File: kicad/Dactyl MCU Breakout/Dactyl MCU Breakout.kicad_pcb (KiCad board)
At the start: 2 copper layers, 54.5 x 62.1 mm, 37 parts, among them J202 Split, J203 Column, J204 Thumb, J205 External, J206 Row, J207 Display, J208 Vic, J209 JST, SW201 Battery, SW202 Reset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

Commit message: feat: four layer PCB, inners GND. Reconnect GNDs.
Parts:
- moved JP201 0.67 mm to (109.5, 84.6)
- moved JP204 0.50 mm to (122.2, 92.4)
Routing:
- net GND: track 45.6 -> 23.0 mm, vias 36 -> 32
- net /Right/RAW_ENABLED: track 3.04 -> 3.58 mm
- added copper zone on In1.Cu, net GND
- added copper zone on In2.Cu, net GND
- removed copper zone on B.Cu, net GND
- removed copper zone on F.Cu, net GND
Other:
- copper layers 2 -> 4
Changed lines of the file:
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@@
 	(layers
 		(0 "F.Cu" signal)
+		(1 "In1.Cu" power)
+		(2 "In2.Cu" power)
 		(31 "B.Cu" signal)
 		(32 "B.Adhes" user "B.Adhesive")
@@
 			)
 			(layer "dielectric 1"
+				(type "prepreg")
+				(thickness 0.1)
+				(material "FR4")
+				(epsilon_r 4.5)
+				(loss_tangent 0.02)
+			)
+			(layer "In1.Cu"
+				(type "copper")
+				(thickness 0.035)
+			)
+			(layer "dielectric 2"
 				(type "core")
-				(thickness 1.51)
+				(thickness 1.24)
+				(material "FR4")
+				(epsilon_r 4.5)
+				(loss_tangent 0.02)
+			)
+			(layer "In2.Cu"
+				(type "copper")
+				(thickness 0.035)
+			)
+			(layer "dielectric 3"
+				(type "prepreg")
+				(thickness 0.1)
 				(material "FR4")
 				(epsilon_r 4.5)
@@
 		(fp_arc
 			(start 6.938123 15.132041)
-			(mid 6.337062 14.8831)
+			(mid 6.337066 14.8831)
 			(end 6.088123 14.282041)
 			(stroke
@@
 		(fp_arc
 			(start 8.236041 -15.740877)
-			(mid 8.837086 -15.491923)
+			(mid 8.837089 -15.491924)
 			(end 9.086041 -14.890877)
 			(stroke
@@
 	(footprint "Dactyl_basics:SolderJumper-2_P1.3mm_Open_RoundedPad1.0x1.5mm"
 		(layer "B.Cu")
-		(at 122.2 92.9 180)
+		(at 122.15 92.4 180)
 		(descr "SMD Solder Jumper, 1x1.5mm, rounded Pads, 0.3mm gap, open")
 		(tags "solder jumper open")
@@
 	(footprint "Dactyl_basics:SolderJumper-2_P1.3mm_Open_RoundedPad1.0x1.5mm"
 		(layer "B.Cu")
-		(at 108.9 84.3 90)
+		(at 109.5 84.6 90)
 		(descr "SMD Solder Jumper, 1x1.5mm, rounded Pads, 0.3mm gap, open")
 		(tags "solder jumper open")
@@
 	)
 	(segment
-		(start 123.5364 56.362)
-		(end 120.938 56.362)
+		(start 121.45 93.95)
+		(end 121.455 93.955)
+		(width 0.381)
+		(layer "F.Cu")
+		(net 2)
+	)
+	(segment
+		(start 105.45 95)
+		(end 104.1625 95)
+		(width 0.381)
+		(layer "F.Cu")
+		(net 2)
+	)
+	(segment
+		(start 105.545 91.85)
+		(end 108.15 91.85)
 		(width 0.381)
 		(layer "F.Cu")
@@
 	)
 	(segment
-		(start 120.9 56.2)
+		(start 120.9 56.5)
 		(end 120.9 55.58)
 		(width 0.381)
@@
 	)
 	(segment
-		(start 118.8 56.35)
-		(end 118.8 57)
+		(start 126.4 101.325305)
+		(end 126.4 102.65)
 		(width 0.381)
 		(layer "F.Cu")
@@
 	)
 	(segment
+		(start 107.4 85.35)
+		(end 105.545 85.35)
+		(width 0.381)
+		(layer "F.Cu")
+		(net 2)
+	)
+	(segment
 		(start 112.2375 80.1)
 		(end 113.8 80.1)
@@
 	)
 	(segment
-		(start 112.65 74.04)
-		(end 112.59 74.1)
+		(start 126.369696 101.295001)
+		(end 126.4 101.325305)
 		(width 0.381)
 		(layer "F.Cu")
@@
 	)
 	(segment
-		(start 120.938 56.362)
-		(end 120.9 56.4)
+		(start 101.5 80.7)
+		(end 100.7 80.7)
 		(width 0.381)
 		(layer "F.Cu")
@@
 	)
 	(segment
-		(start 119.1 57.3)
-		(end 119.8 57.3)
+		(start 127.7 62.8)
+		(end 126.78 62.8)
 		(width 0.381)
 		(layer "F.Cu")
@@
 	)
 	(segment
-		(start 118.8 57)
-		(end 119.1 57.3)
+		(start 108.1 84.65)
+		(end 107.4 85.35)
 		(width 0.381)
 		(layer "F.Cu")
@@
 	)
 	(segment
-		(start 112.59 74.1)
-		(end 107.325 74.1)
+		(start 118.8 57.5)
+		(end 118.8 56.35)
+		(width 0.381)
+		(layer "F.Cu")
+		(net 2)
+	)
+	(segment
+		(start 128.5 95.325)
+		(end 128.5 94.05)
 		(width 0.381)
 		(layer "F.Cu")
@@
 	)
 	(segment
-		(start 119.8 57.3)
-		(end 120.9 56.2)
+		(start 121.455 93.955)
+		(end 121.455 95.325)
 		(width 0.381)
 		(layer "F.Cu")
@@
 	)
 	(via
-		(at 138.9 103.65)
-		(size 0.8)
-		(drill 0.4)
-		(layers "F.Cu" "B.Cu")
-		(free yes)
-		(net 2)
-	)
-	(via
 		(at 114.7 81.6)
 		(size 0.8)
@@
 	)
 	(via
-		(at 132.2 60.25)
-		(size 0.8)
-		(drill 0.4)
-		(layers "F.Cu" "B.Cu")
-		(free yes)
-		(net 2)
-	)
-	(via
-		(at 119.75 96)
+		(at 121.45 93.95)
 		(size 0.8)
 		(drill 0.4)
@@
 	)
 	(via
-		(at 125.3 99.3)
+		(at 126.369696 101.295001)
 		(size 0.8)
 		(drill 0.4)
@@
 	)
 	(via
-		(at 132.2 58)
+		(at 105.45 95)
 		(size 0.8)
 		(drill 0.4)
@@
 	)
 	(via
-		(at 112.65 74.04)
+		(at 107.325 74.1)
 		(size 0.8)
 		(drill 0.4)
@@
 	)
 	(via
-		(at 101.85 79)
+		(at 100.7 80.7)
 		(size 0.8)
 		(drill 0.4)
@@
 	)
 	(via
-		(at 126.675 95.15)
+		(at 128.5 94.05)
 		(size 0.8)
 		(drill 0.4)
@@
 	)
 	(via
-		(at 122.8 90.4)
+		(at 120.9 56.5)
 		(size 0.8)
 		(drill 0.4)
@@
 	)
 	(via
-		(at 147.9 93.1)
+		(at 122.8 90.4)
 		(size 0.8)
 		(drill 0.4)
@@
 	)
 	(via
-		(at 128.6 60.25)
+		(at 147.9 93.1)
 		(size 0.8)
 		(drill 0.4)
@@
 	)
 	(via
-		(at 108.75 93.9)
+		(at 108.15 91.85)
 		(size 0.8)
 		(drill 0.4)
@@
 	)
 	(via
-		(at 101.75 88.65)
+		(at 108.1 84.65)
 		(size 0.8)
 		(drill 0.4)
@@
 	)
 	(via
-		(at 132.2 54.6)
-		(size 0.8)
-		(drill 0.4)
-		(layers "F.Cu" "B.Cu")
-		(free yes)
-		(net 2)
-	)
-	(via
-		(at 138.9 99.15)
+		(at 118.8 57.5)
 		(size 0.8)
 		(drill 0.4)
@@
 	)
 	(via
-		(at 116.4 57.1)
-		(size 0.8)
-		(drill 0.4)
-		(layers "F.Cu" "B.Cu")
-		(free yes)
-		(net 2)
-	)
-	(via
-		(at 126.7 60.25)
+		(at 127.7 62.8)
 		(size 0.8)
 		(drill 0.4)
@@
 	)
 	(segment
-		(start 123.5364 56.362)
-		(end 121.363 56.362)
-		(width 0.381)
-		(layer "B.Cu")
-		(net 2)
-	)
-	(segment
-		(start 121.363 56.362)
-		(end 120 57.725)
-		(width 0.381)
-		(layer "B.Cu")
-		(net 2)
-	)
-	(segment
-		(start 113.72 64.88)
-		(end 116.4 64.88)
-		(width 0.381)
-		(layer "B.Cu")
-		(net 2)
-	)
-	(segment
-		(start 112.675 74.015)
-		(end 112.675 65.925)
-		(width 0.381)
-		(layer "B.Cu")
-		(net 2)
-	)
-	(segment
-		(start 112.675 65.925)
-		(end 113.72 64.88)
-		(width 0.381)
-		(layer "B.Cu")
-		(net 2)
-	)
-	(segment
-		(start 116.6 64.88)
-		(end 116.4 64.88)
-		(width 0.381)
-		(layer "B.Cu")
-		(net 2)
-	)
-	(segment
-		(start 120 57.725)
-		(end 120 61.48)
-		(width 0.381)
-		(layer "B.Cu")
-		(net 2)
-	)
-	(segment
-		(start 112.65 74.04)
-		(end 112.675 74.015)
-		(width 0.381)
-		(layer "B.Cu")
-		(net 2)
-	)
-	(segment
-		(start 120 61.48)
-		(end 116.6 64.88)
-		(width 0.381)
-		(layer "B.Cu")
-		(net 2)
-	)
-	(segment
 		(start 115.185 101.65)
 		(end 113.38 103.455)
@@
 	)
 	(segment
-		(start 120.7 92.9)
-		(end 121.55 92.9)
-		(width 0.25)
-		(layer "B.Cu")
-		(net 5)
-	)
-	(segment
 		(start 102 72)
 		(end 101.675 71.675)
@@
 	)
 	(segment
+		(start 118.2 95.1)
+		(end 120.9 92.4)
+		(width 0.25)
+		(layer "B.Cu")
+		(net 5)
+	)
+	(segment
 		(start 118.2 97.5)
-		(end 115 100.7)
+		(end 118.2 95.1)
 		(width 0.25)
 		(layer "B.Cu")
@@
 	(segment
 		(start 118.2 97.5)
-		(end 118.2 95.4)
+		(end 115 100.7)
 		(width 0.25)
 		(layer "B.Cu")
@@
 	)
 	(segment
-		(start 118.2 95.4)
-		(end 120.7 92.9)
+		(start 120.9 92.4)
+		(end 121.5 92.4)
 		(width 0.25)
 		(layer "B.Cu")
@@
 	)
 	(segment
-		(start 108.35 86.15)
-		(end 108.9 85.6)
+		(start 108.3 86.15)
+		(end 109.25 86.15)
 		(width 0.381)
 		(layer "B.Cu")
@@
 	)
 	(segment
-		(start 108.9 85.6)
-		(end 108.9 84.95)
+		(start 109.5 85.9)
+		(end 109.5 85.25)
 		(width 0.381)
 		(layer "B.Cu")
@@
 	)
 	(segment
-		(start 108.3 86.15)
-		(end 108.35 86.15)
+		(start 109.25 86.15)
+		(end 109.5 85.9)
 		(width 0.381)
 		(layer "B.Cu")
@@
 	(segment
 		(start 126.1 92.9)
-		(end 122.85 92.9)
+		(end 125.6 92.4)
+		(width 0.25)
+		(layer "B.Cu")
+		(net 37)
+	)
+	(segment
+		(start 125.6 92.4)
+		(end 122.8 92.4)
 		(width 0.25)
 		(layer "B.Cu")
@@
 	)
 	(segment
-		(start 108.9 82.2)
+		(start 109.5 82.8)
 		(end 108.8 82.1)
 		(width 0.381)
@@
 	)
 	(segment
-		(start 108.9 83.65)
-		(end 108.9 82.2)
+		(start 109.5 83.95)
+		(end 109.5 82.8)
 		(width 0.381)
 		(layer "B.Cu")
@@
 		(net_name "GND")
 		(locked yes)
-		(layers "F&B.Cu")
+		(layers "In1.Cu" "In2.Cu")
 		(name "GND")
 		(hatch edge 0.5)

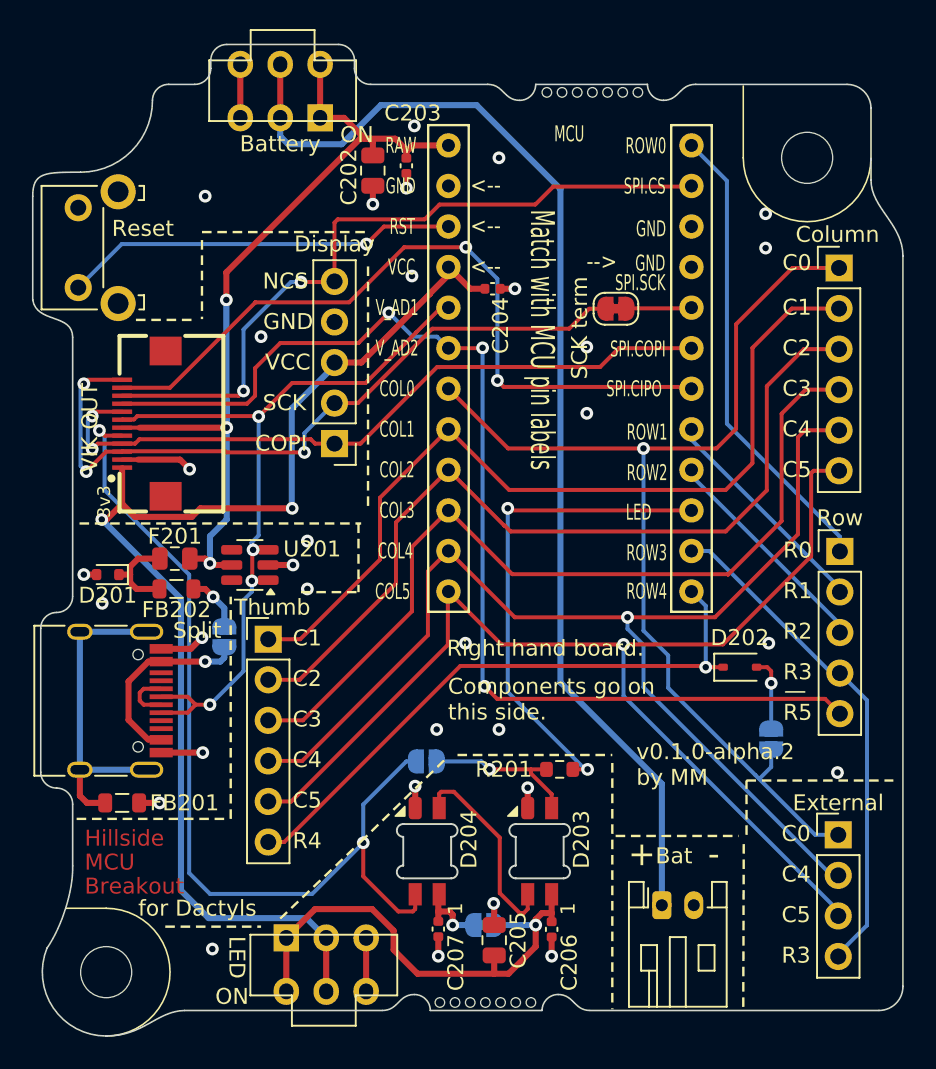
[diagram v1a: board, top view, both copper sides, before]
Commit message: feat: simplify traces, reduce trace vias. stitch
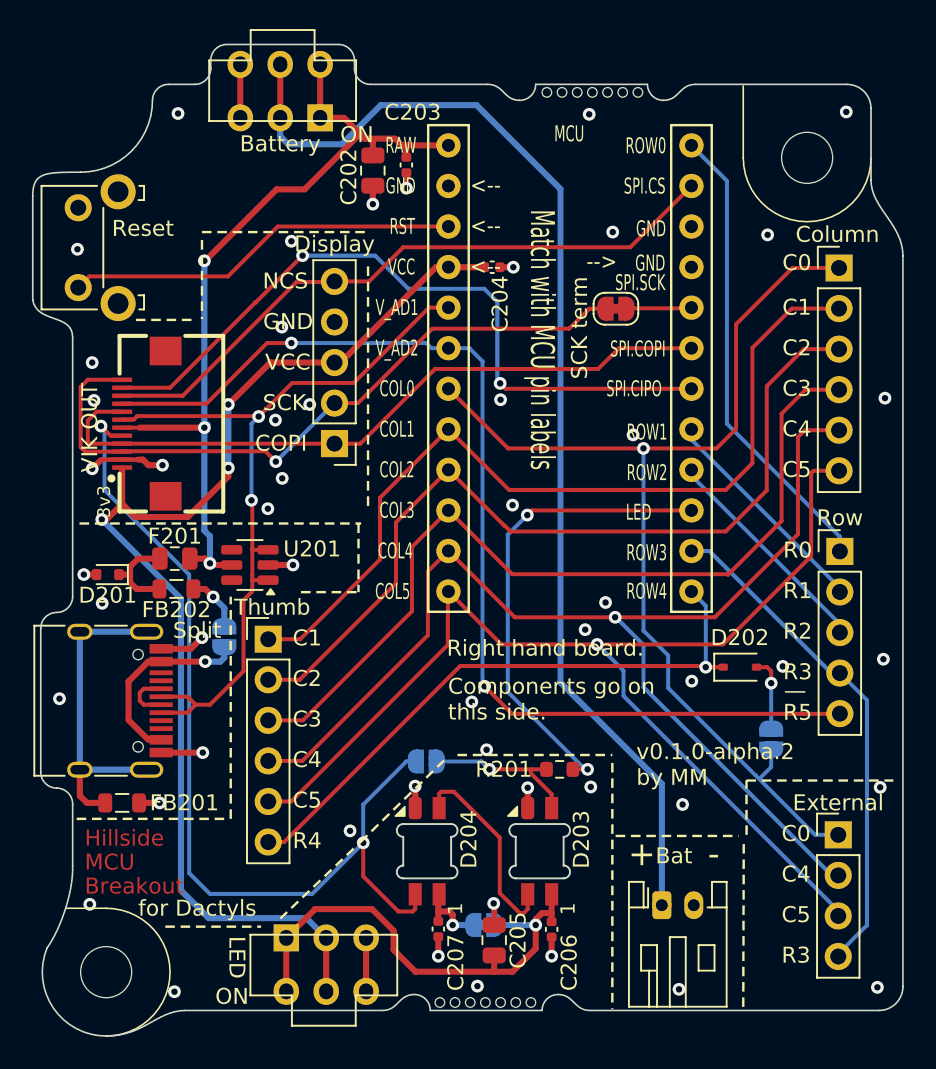
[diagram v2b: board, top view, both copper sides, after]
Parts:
- moved C204 1.35 mm to (126.3, 61.5)
- moved C203 0.05 mm to (120.9, 55.0)
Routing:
- net /Right/SPI0.SC: track 45.5 -> 41.1 mm, vias 2 -> 0
- net /Right/row5_VIK_GP_AD2: track 71.1 -> 68.0 mm, vias 3 -> 2
- net /Right/VCC: track 73.5 -> 71.3 mm, vias 2 -> 3
- net /Right/SPI0.SCK/SDA: track 45.8 -> 43.8 mm, vias 3 -> 1
- net /Right/RAW: track 52.8 -> 51.0 mm
- net /Right/SPI0.CIPO: track 46.7 -> 45.4 mm
- net /Right/LED: track 31.1 -> 29.9 mm
- net /Right/col5: track 74.6 -> 75.3 mm
- net /Right/SPI0.COPI/SCL: track 44.7 -> 44.1 mm, vias 2 -> 0
- net GND: track 23.0 -> 23.3 mm, vias 32 -> 51
- net /Right/SPLIT_VIK_GP_AD1: track 50.2 -> 50.3 mm, vias 4 -> 2
- net /Right/RST: vias 1 -> 0

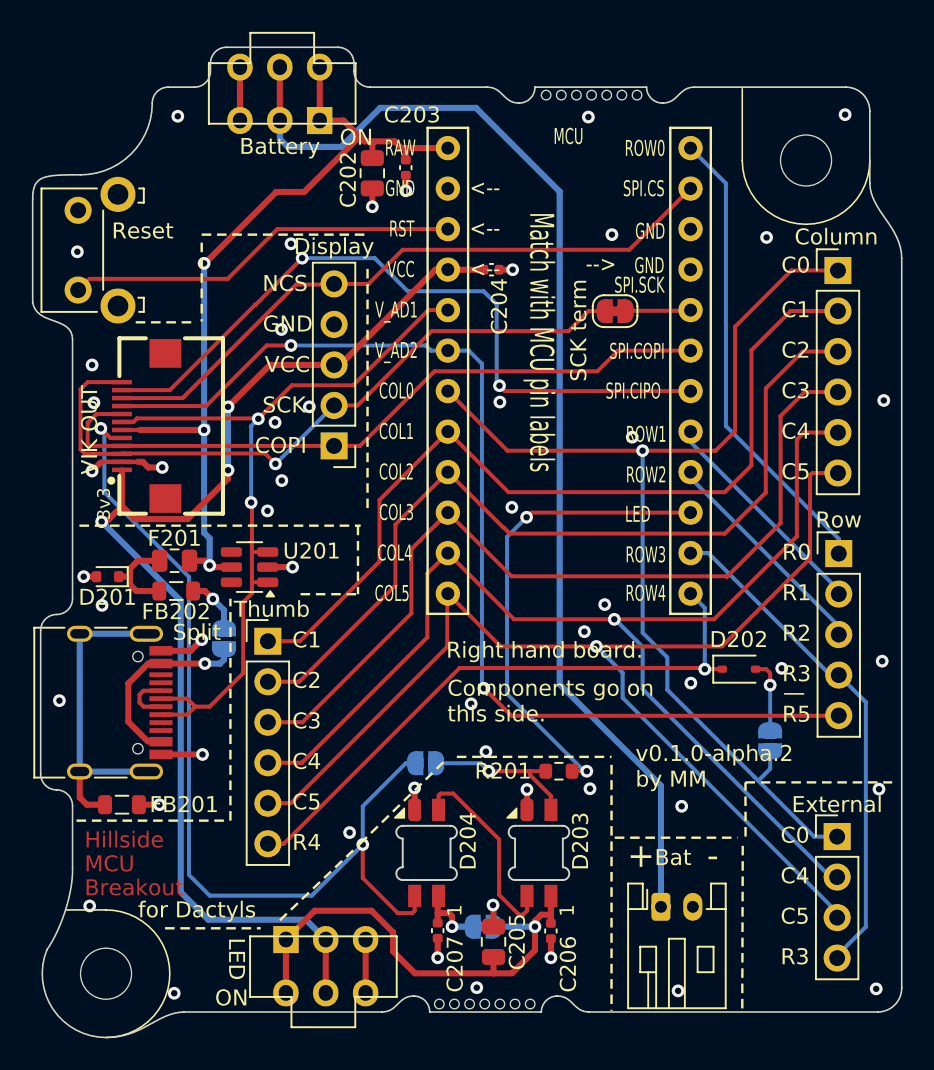
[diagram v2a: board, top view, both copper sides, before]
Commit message: feat: shrink width so two fit in 100 mm wide panel
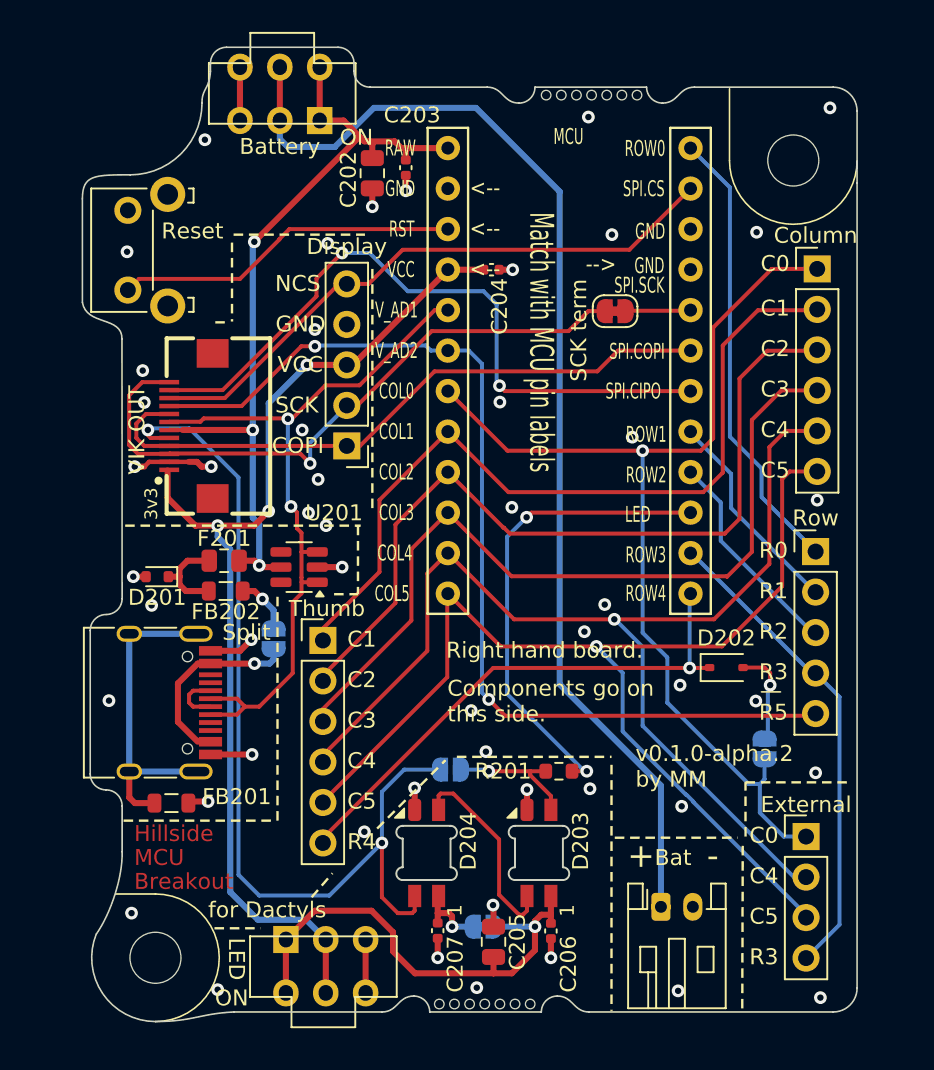
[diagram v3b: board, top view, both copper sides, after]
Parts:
- moved J204 3.45 mm to (115.7, 84.7)
- moved H202 3.26 mm to (105.2, 104.6)
- moved REF** 3.13 mm to (107.1, 98.4)
- moved SW202 3.12 mm to (104.7, 60.2)
- moved U201 3.11 mm to (114.2, 80.1)
- moved D201 3.11 mm to (105.3, 80.7)
- moved F201 3.11 mm to (109.5, 79.7)
- moved FB202 3.11 mm to (109.6, 81.6)
- moved J202 3.11 mm to (104.6, 88.6)
- moved JP201 3.11 mm to (112.6, 84.6)
- moved FB201 3.10 mm to (106.2, 94.9)
- moved J208 2.96 mm to (108.1, 71.2)
- moved J205 1.95 mm to (146.0, 97.0)
- moved JP204 1.60 mm to (123.7, 92.8)
- moved J206 1.46 mm to (146.6, 79.1)
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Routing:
- net /Right/VCC: track 71.3 -> 64.0 mm
- net /Right/row4: track 38.2 -> 33.7 mm
- net /Right/row5_VIK_GP_AD2: track 68.0 -> 63.9 mm
- net /Right/col4: track 75.9 -> 72.0 mm
- net /Right/col5: track 75.3 -> 71.8 mm
- net /Right/col1: track 54.0 -> 50.5 mm
- net /Right/SPI0.COPI/SCL: track 44.1 -> 40.7 mm
- net /Right/RST: track 24.8 -> 21.7 mm
- net /Right/col3: track 54.0 -> 50.9 mm
- net /Right/SPI0.SC: track 41.1 -> 38.1 mm
- net /Right/SPLIT_VIK_GP_AD1: track 50.3 -> 47.5 mm
- net /Right/SPI0.SCK/SDA: track 43.8 -> 41.0 mm
- net /Right/col2: track 53.6 -> 51.1 mm
- net /Right/RAW: track 51.0 -> 48.5 mm
- net /Right/SPI0.CIPO: track 45.4 -> 43.4 mm
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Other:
- board size 54.5 x 62.1 mm -> 48.6 x 61.1 mm
